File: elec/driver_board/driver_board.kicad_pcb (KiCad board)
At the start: 2 copper layers, 226.2 x 90.5 mm, 131 parts, among them J1 rotary_encoder, J2 DCF77 board, J3 RTC, M1 Conn motor 0, M10 Conn motor 1, M11 Conn motor 0, M12 Conn motor 1, M13 Conn motor 0, M14 Conn motor 1, M15 Conn motor 0, M16 Conn motor 1, M17 Conn motor 0, M18 Conn motor 1, M19 Conn motor 0, M2 Conn motor 1, M20 Conn motor 1, M21 Conn motor 0, M22 Conn motor 1, M23 Conn motor 0, M24 Conn motor 1, M3 Conn motor 0, M4 Conn motor 1, M5 Conn motor 0, M6 Conn motor 1, M7 Conn motor 0, M8 Conn motor 1, M9 Conn motor 0, U1 ESP32-C3-DEVKITM-1, U10 VID6606, U11 74HCT595, U12 VID6606, U13 74HCT595, U14 VID6606, U15 74HCT595, U16 VID6606, U17 74HCT595, U18 VID6606, U19 74HCT595, U2 TXB0102DCT, U20 VID6606, U21 74HCT595, U22 VID6606, U23 74HCT595, U24 VID6606, U25 74HCT595, U26 VID6606, U3 74HCT595, U4 VID6606, U5 74HCT595, U6 VID6606, U7 74HCT595, U8 VID6606, U9 74HCT595

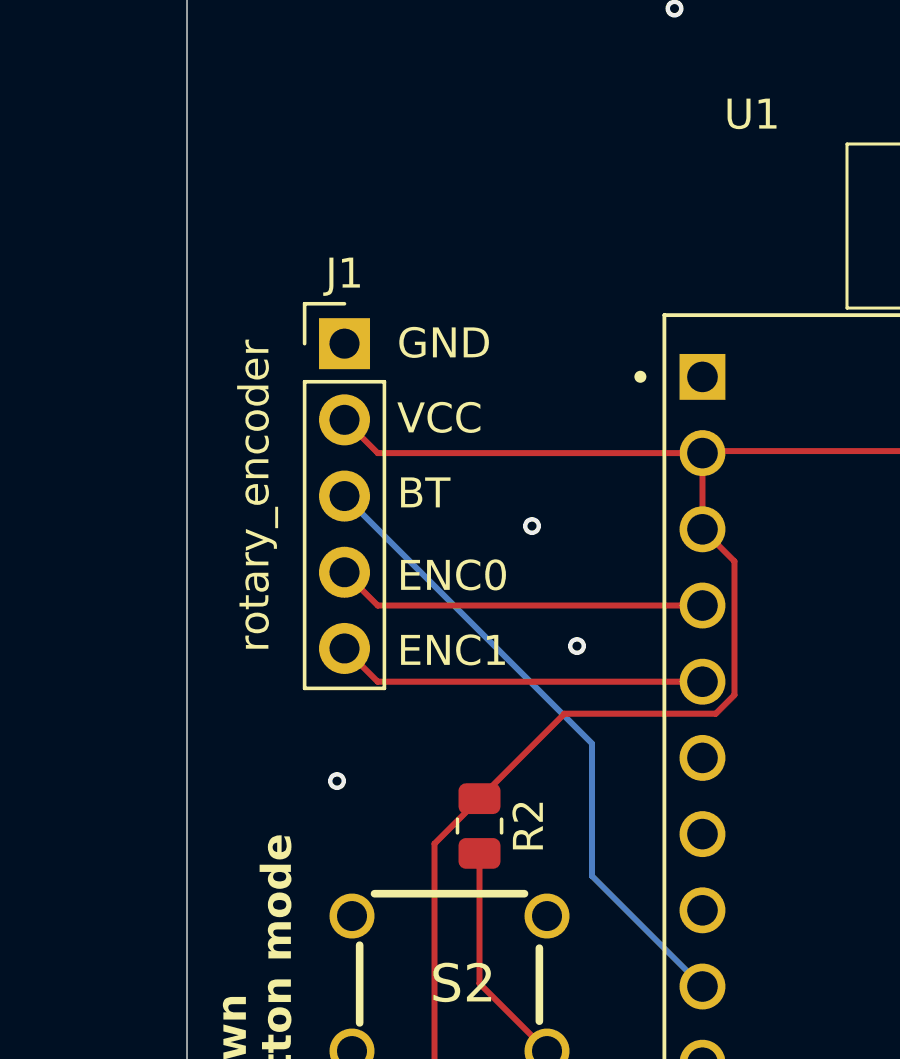
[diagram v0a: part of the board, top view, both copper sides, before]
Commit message: Update hole size
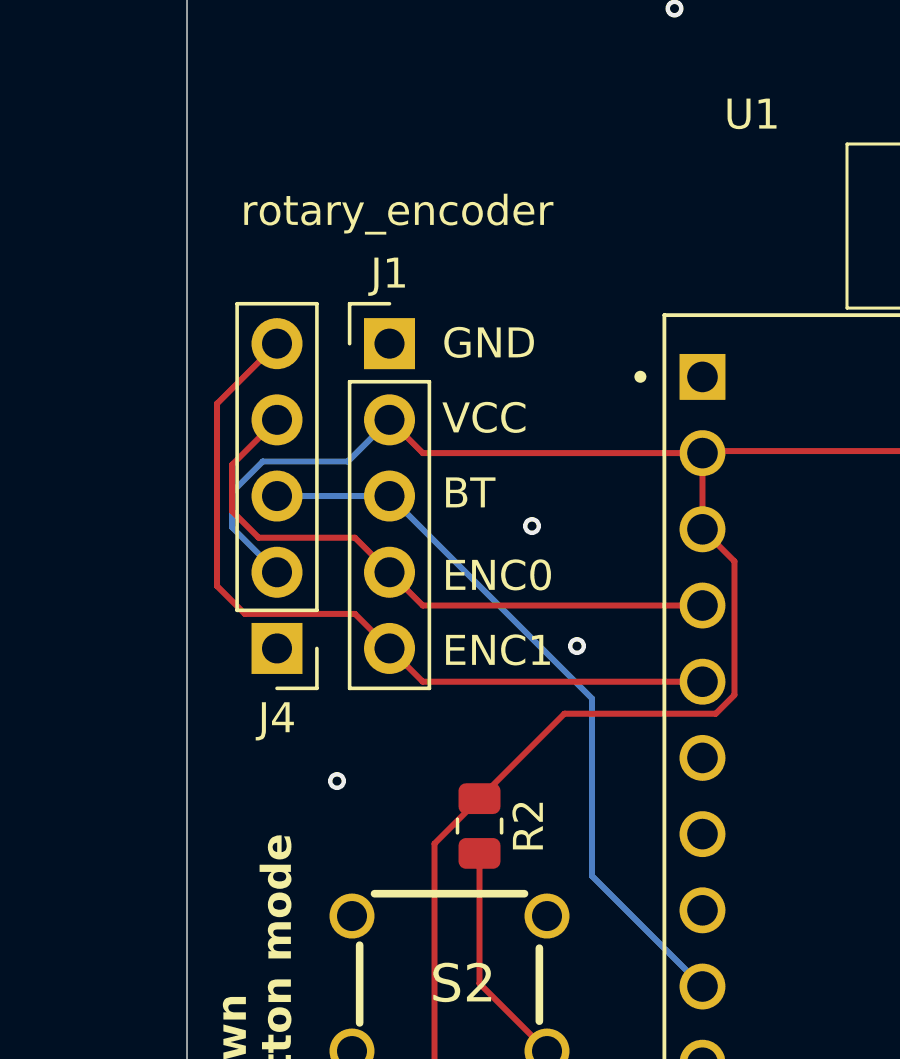
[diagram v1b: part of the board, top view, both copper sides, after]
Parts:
- added J4: rotary_encoder, Connector_PinHeader_2.54mm:PinHeader_1x05_P2.54mm_Vertical, F.Cu at (44.5, 76.6)
- moved J1 1.50 mm to (48.2, 66.4)
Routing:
- net /control_board/PIN_ENCODER_1: track 12.4 -> 26.4 mm
- net /control_board/PIN_ENCODER_0: track 12.4 -> 20.6 mm
- net /control_board/VCC_3V3: track 111.9 -> 120.0 mm
- net /control_board/PIN_BUTTON_ENCODER: track 21.3 -> 24.4 mm

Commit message: Finalize PCB order
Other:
- board text added: "Clockclock v2.1 Tibo 27/02/2025"
- board text removed: "Clockclock v2.1 Tibo 26/02/2025"
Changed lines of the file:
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@@
 		)
 	)
-	(gr_text "Clockclock v2.1\nTibo 26/02/2025"
+	(gr_text "Clockclock v2.1\nTibo 27/02/2025"
 		(at 150.25 88 0)
 		(layer "F.SilkS")
